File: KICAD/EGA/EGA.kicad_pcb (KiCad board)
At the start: 2 copper layers, 39 parts, among them J1 12V, J10 TEST_TRIG, J2 HC-SR04, J3 LCD 20x4, J4 RTC, J5 TEST_PWM, J6 FAN_12V_PWM_3.3V, J7 UART, J8 TEST_RPM, J9 TEST_ECHO, SW1 PAGINA, SW2 RESET, U1 LM7805_TO220, U2 LM317_TO-220, U3 Pico

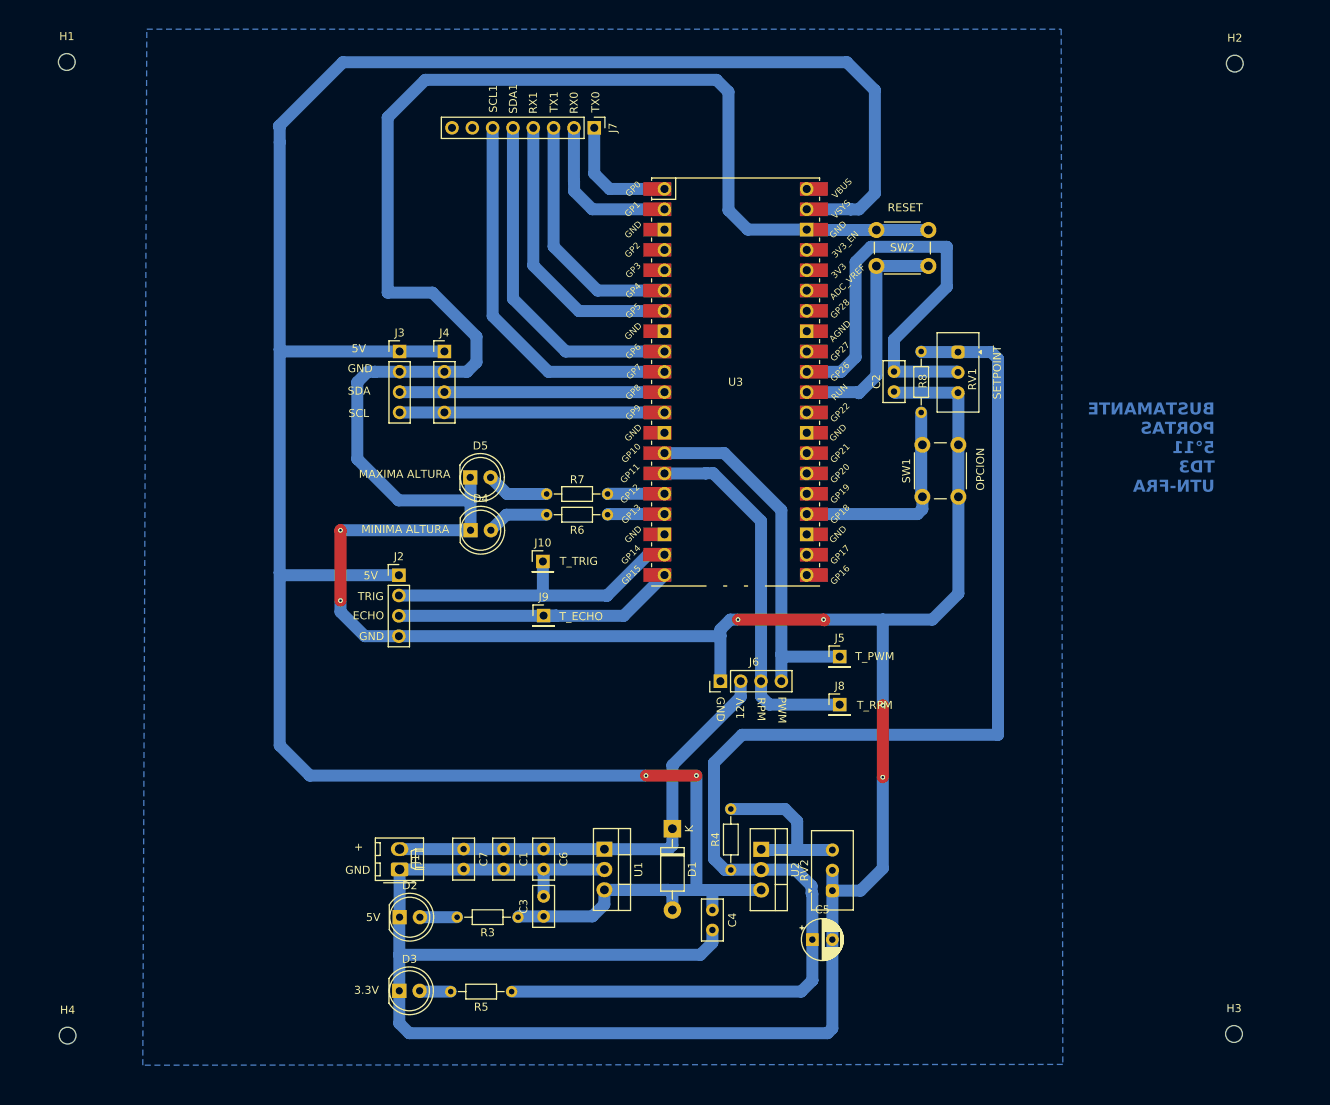
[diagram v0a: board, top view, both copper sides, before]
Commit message: Actualizacion de Kicad, Adicion de manual de usuario
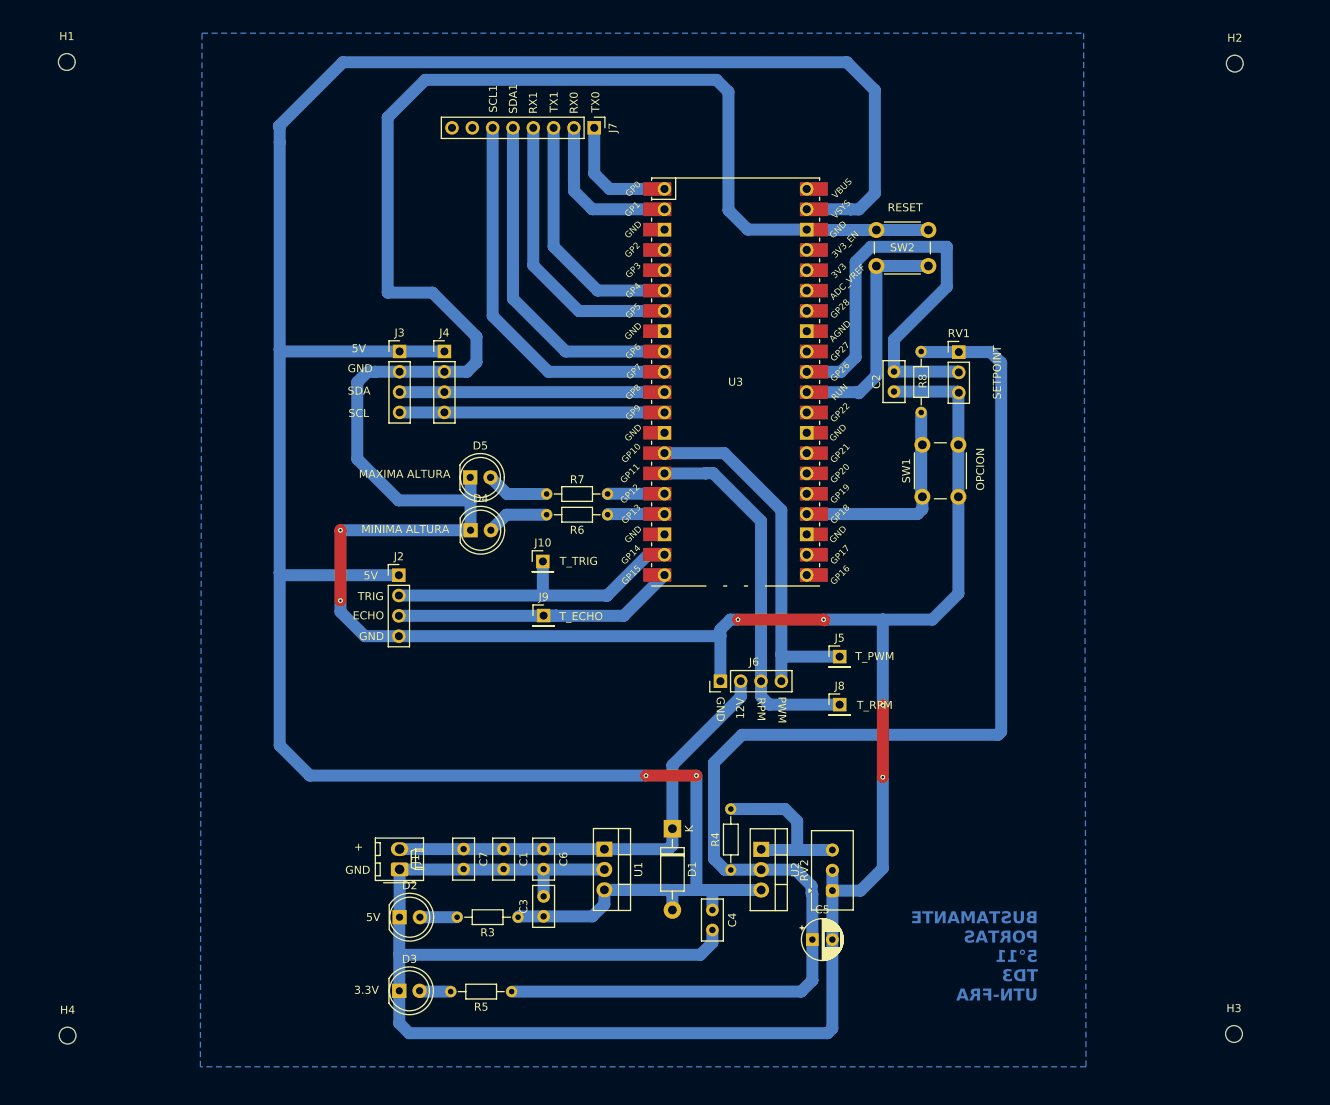
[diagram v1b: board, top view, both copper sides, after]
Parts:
- RV1: footprint Potentiometer_THT:Potentiometer_Vishay_T93XA_Horizontal -> Connector_PinHeader_2.54mm:PinHeader_1x03_P2.54mm_Vertical
- moved RV1 0.10 mm to (154.8, 66.7), turned to 0 degrees

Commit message: Actualizacion de informe
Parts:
- H1: value MountingHole -> SD
- H2: value MountingHole -> SI
- H3: value MountingHole -> ID
- H4: value MountingHole -> II
- RV1: footprint Connector_PinHeader_2.54mm:PinHeader_1x03_P2.54mm_Vertical -> Potentiometer_THT:Potentiometer_Vishay_T93XA_Horizontal
- moved RV1 4.60 mm to (159.4, 66.7), turned to -90 degrees
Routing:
- net 3.3V: track 169.9 -> 122.5 mm
- net GND: track 522.7 -> 527.5 mm
- net PIN_ADC: track 57.6 -> 62.1 mm
- removed copper zone on B.Cu, net GND
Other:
- board outline added: 162.2 x 134 mm

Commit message: features/Rama Agregado de SD
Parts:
- removed RV1: SetPoint, Potentiometer_THT:Potentiometer_Vishay_T93XA_Horizontal
- added J11: POTENCIOMETRO, Connector_PinHeader_2.54mm:PinHeader_1x03_P2.54mm_Vertical, F.Cu at (156.2, 67.9)
- J7: footprint Connector_PinHeader_2.54mm:PinHeader_1x08_P2.54mm_Vertical -> Connector_PinHeader_2.54mm:PinHeader_1x10_P2.54mm_Vertical
- SW1, SW2: footprint Button_Switch_THT:SW_PUSH_6mm_H5mm -> Button_Switch_THT:SW_PUSH_6mm_H8mm
- moved J7 17.9 mm to (91.9, 33.9), turned to 0 degrees
- moved R3 4.12 mm to (101.2, 133.4)
- moved C4 4.12 mm to (125.4, 132.5)
- moved D2 4.12 mm to (86.3, 133.4)
- moved U1 4.12 mm to (111.9, 124.9)
- moved D4 4.12 mm to (95.2, 85.1)
- moved R4 4.12 mm to (127.7, 127.5)
- moved D5 4.12 mm to (95.2, 78.5)
- moved J10 4.12 mm to (104.3, 89.0)
- moved J2 4.12 mm to (86.3, 90.7)
- moved J5 4.12 mm to (141.4, 100.9)
- moved J6 4.12 mm to (126.4, 103.9)
- moved J8 4.12 mm to (141.4, 106.9)
- moved R7 4.12 mm to (112.3, 80.5)
- moved R8 4.12 mm to (151.5, 62.7)
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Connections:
- J7 pad 1: UART0_TX -> 5V
- J7 pad 2: UART0_RX -> RX/SPI0
- J7 pad 3: UART1_TX -> CSn/SPI0
- J7 pad 4: UART1_RX -> GND
- J7 pad 5: SDA_1 -> SCK/SPI0
- J7 pad 6: SCL_1 -> TX/SPI0
- J7 pad 7: unconnected-(J7-Pin_7-Pad7) -> UART1_TX
- J7 pad 8: unconnected-(J7-Pin_8-Pad8) -> UART1_RX
- SW2 pad 2: GND -> Net-(SW2-Pad2)
- U3 pad 1: UART0_TX -> RX/SPI0
- U3 pad 2: UART0_RX -> CSn/SPI0
- U3 pad 3: unconnected-(U3-GND-Pad3) -> GND
- U3 pad 38: GND -> Net-(SW2-Pad2)
- U3 pad 4: unconnected-(U3-GPIO2-Pad4)_0 -> SCK/SPI0
- U3 pad 5: unconnected-(U3-GPIO3-Pad5) -> TX/SPI0
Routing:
- net GND: track 527.5 -> 470.0 mm
- net 3.3V: track 122.5 -> 170.2 mm
- net RX/SPI0: track 0.00 -> 31.8 mm
- net SCK/SPI0: track 0.00 -> 31.8 mm
- net CSn/SPI0: track 0.00 -> 31.8 mm
- net 5V: track 328.9 -> 297.5 mm
- net TX/SPI0: track 0.00 -> 31.2 mm
- net UART0_RX: track 20.2 -> 0.00 mm
- net SCL_1: track 47.9 -> 31.1 mm
- net Net-(SW2-Pad2): track 0.00 -> 15.3 mm
- net UART0_TX: track 15.3 -> 0.00 mm
- net SDA_1: track 43.0 -> 31.1 mm
- net UART1_RX: track 36.0 -> 30.2 mm
- net PIN_ADC: track 62.1 -> 57.4 mm
- net UART1_TX: track 31.0 -> 30.0 mm
- added copper zone on B.Cu, net GND
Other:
- board text added: "CSn"
- board text added: "RX"
- board text added: "RX_UART"
- board text added: "SCK"
- board text added: "SCL_1"
- board text added: "SDA_1"
- board text added: "TX"
- board text added: "TX_UART"
- board text removed: "RX0"
- board text removed: "RX1"
- board text removed: "SCL1"
- board text removed: "SDA1"
- board text removed: "TX0"
- board text removed: "TX1"

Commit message: Version de entrega V1
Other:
- board text added: "RX/MISO"
- board text added: "TX/MOSI"
- board text removed: "RX"
- board text removed: "TX"
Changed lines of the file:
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@@
 		)
 		(fp_text user "${REFERENCE}"
-			(at 0 2.54 270)
+			(at 0 2.54 -90)
 			(layer "F.Fab")
 			(effects
@@
 		)
 	)
-	(gr_text "RX"
-		(at 88.945 36.395 0)
+	(gr_text "RX/MISO"
+		(at 86.75 36.395 0)
 		(layer "F.SilkS")
 		(effects
@@
 		)
 	)
-	(gr_text "TX"
-		(at 88.945 46.645 0)
-		(layer "F.SilkS")
-		(effects
+	(gr_text "TX/MOSI"
+		(at 86.75 46.5 0)
+		(layer "F.SilkS")
+		(effects
